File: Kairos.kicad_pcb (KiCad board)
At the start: 2 copper layers, 285 x 94.6 mm, 143 parts, among them Q1 NSS40301MZ4T1G, SW1 SW_RST1, U1 ATMEGA32U2-AU, Y1 Crystal_GND24

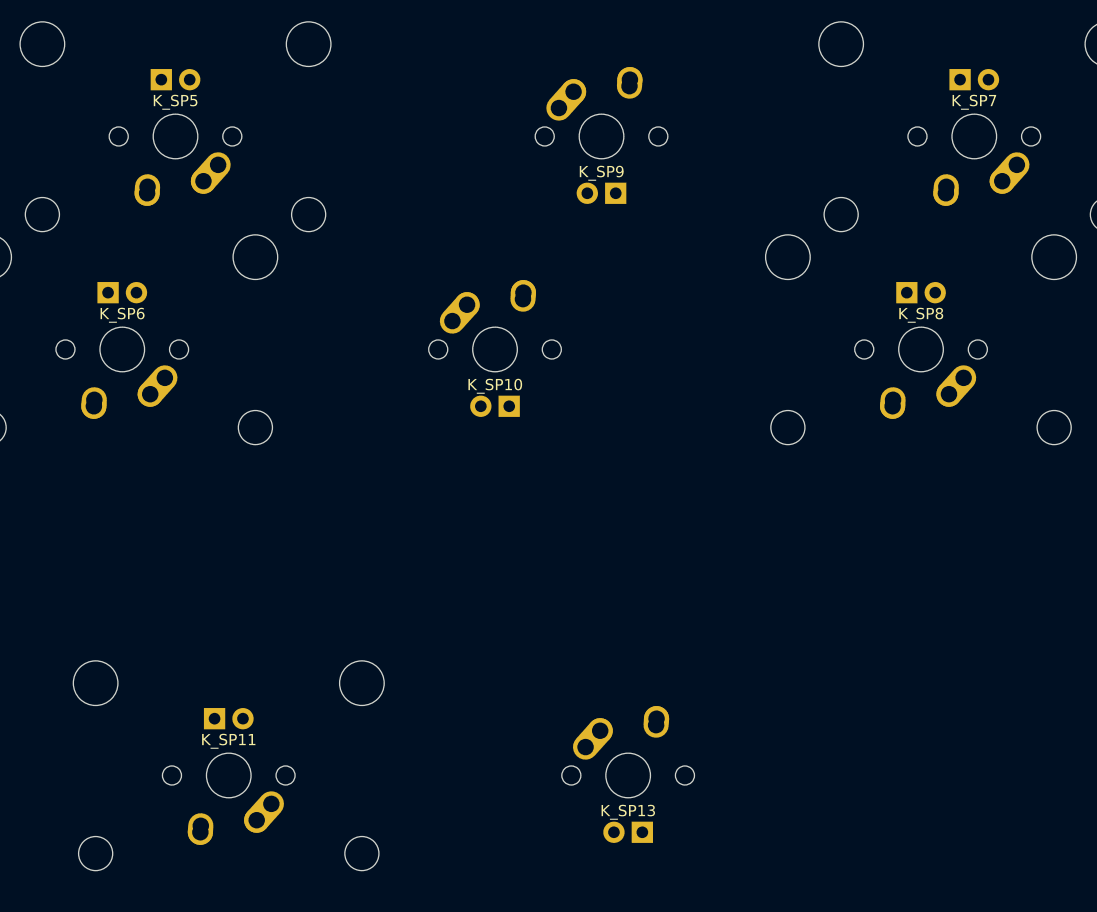
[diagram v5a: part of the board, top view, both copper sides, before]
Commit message: Fix 2.25 and 2.75U flipped stabilizer holes
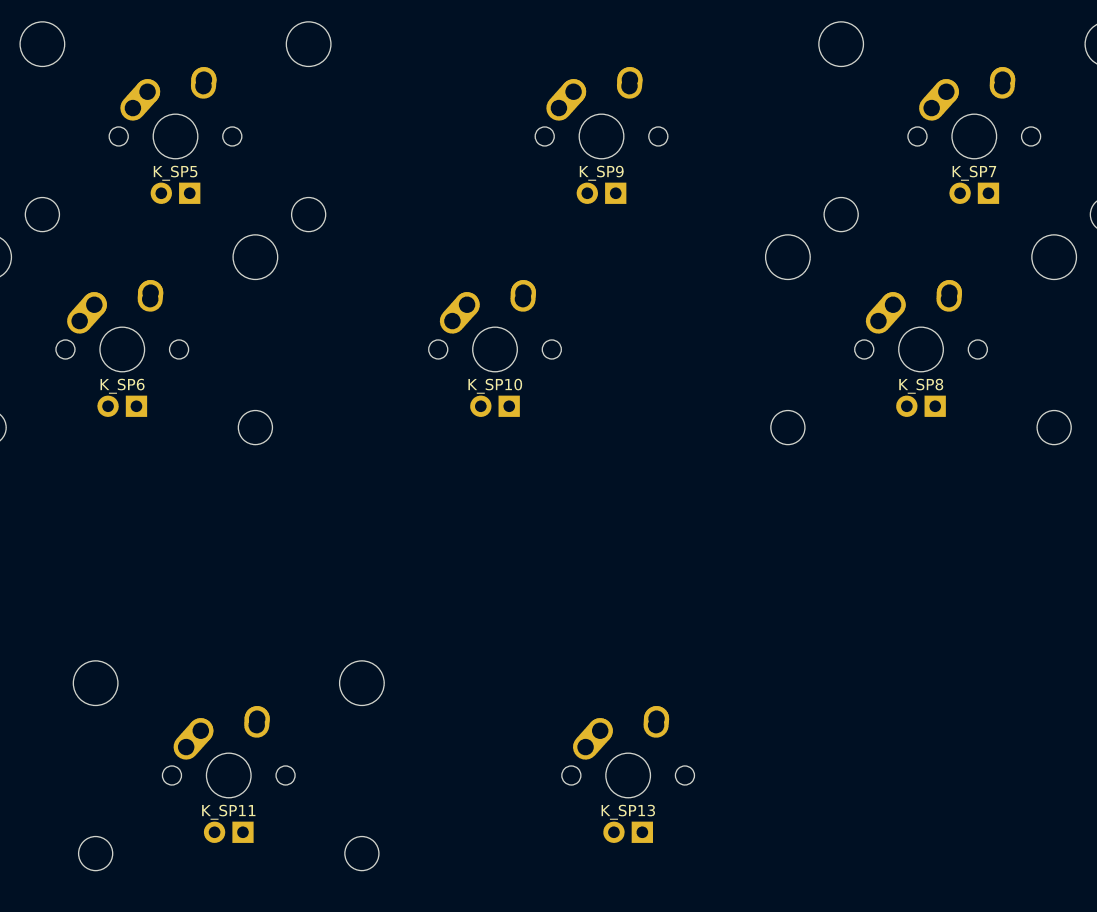
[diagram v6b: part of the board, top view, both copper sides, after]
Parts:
- K_SP11, K_SP5, K_SP8: footprint MX_Alps_Hybrid:MX-2.75U -> MX_Alps_Hybrid:MX-2.75U-ReversedStabilizer
- K_SP6, K_SP7: footprint MX_Alps_Hybrid:MX-2.25U -> MX_Alps_Hybrid:MX-2.25U-ReversedStabilizer
- turned K_SP11 to 0 degrees
- turned K_SP5 to 0 degrees
- turned K_SP6 to 0 degrees
- turned K_SP7 to 0 degrees
- turned K_SP8 to 0 degrees

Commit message: Remove the two keys on PCB
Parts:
- removed K_LM5: MX-1.5U, MX_Alps_Hybrid:MX-1.5U
- removed K_SP1: MX-7U, MX_Alps_Hybrid:MX-7U-ReversedStabilizers

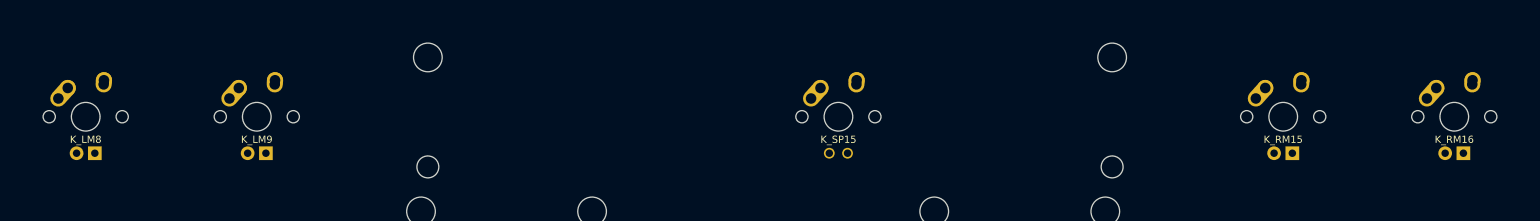
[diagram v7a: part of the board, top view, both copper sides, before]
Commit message: Remove true HHKB row (LM8/9, SP15, RM15/16)
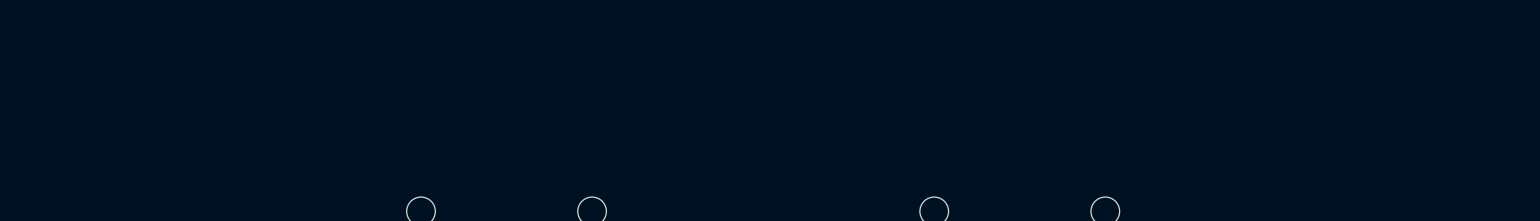
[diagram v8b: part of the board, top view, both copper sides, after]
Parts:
- removed K_LM8, K_RM16: MX-1U, MX_Alps_Hybrid:MX-1U
- removed K_LM9, K_RM15: MX-1.5U, MX_Alps_Hybrid:MX-1.5U
- removed K_SP15: MX-6U, MX_Alps_Hybrid:MX-6U
